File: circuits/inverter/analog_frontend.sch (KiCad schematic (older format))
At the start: 104 parts

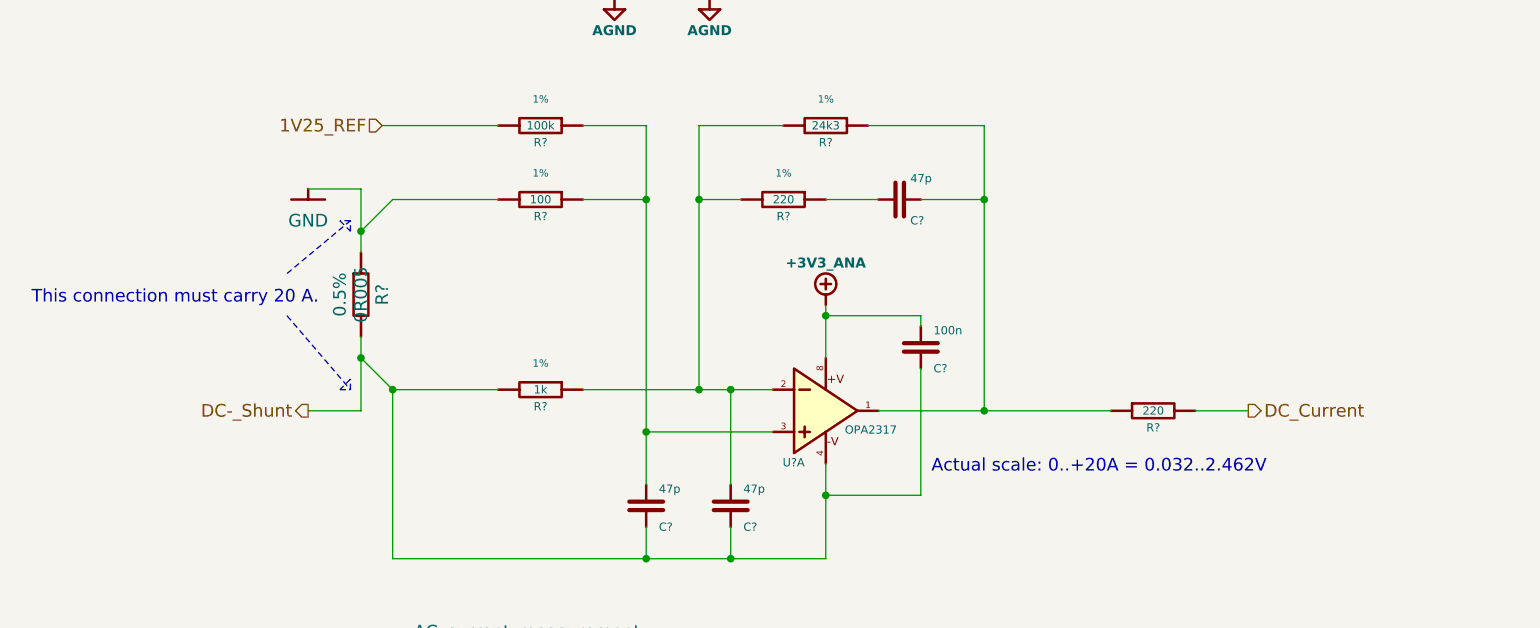
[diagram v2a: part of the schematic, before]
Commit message: fixes power symbols and pin attributes in library,
adds various footprints
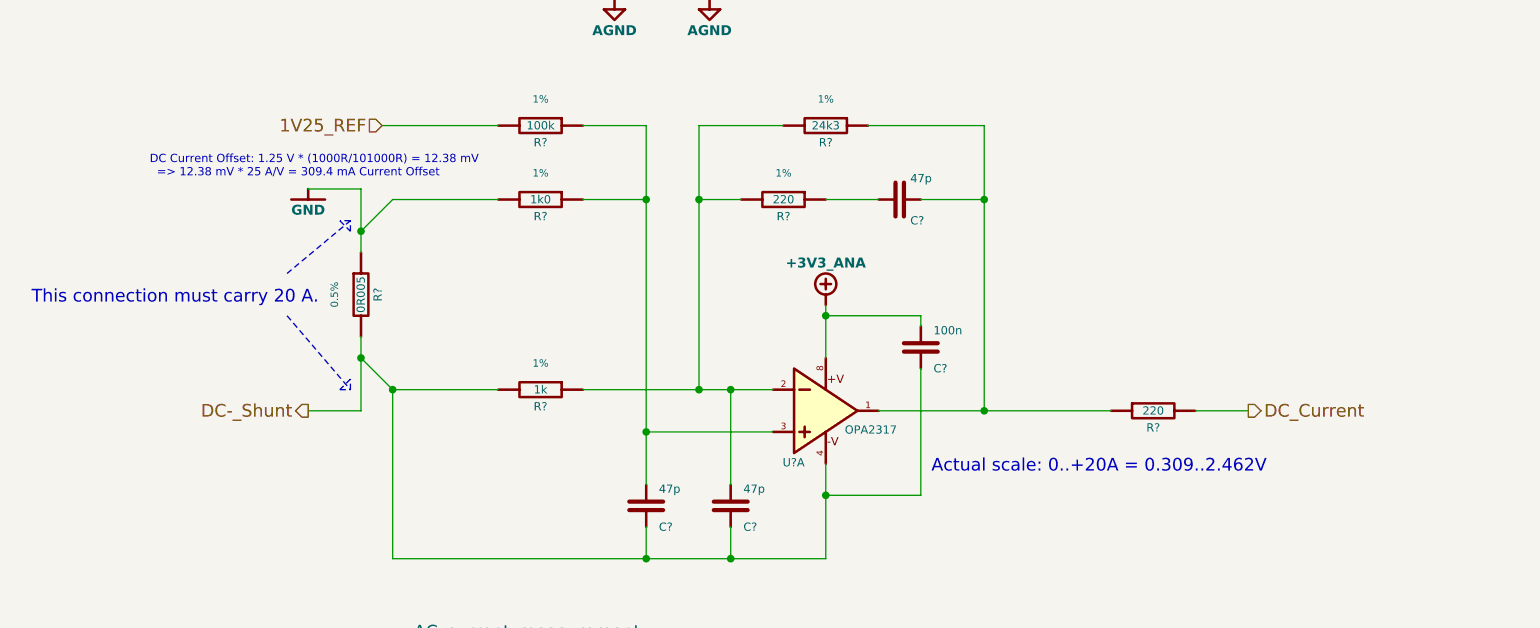
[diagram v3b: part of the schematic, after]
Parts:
- removed R?: 0R005, symbol Resistor
- added R?: 0R005, symbol Resistor
- R?: value 100 -> 1k0
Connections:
- net DC-_Shunt: now also R?.2
- net at R?.2: now also R?.1
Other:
- note added: "Actual scale: 0..+20A = 0.309..2.462V"
- note added: "DC Current Offset: 1.25 V * (1000R/101000R) = 12.38 mV\n => 12.38 mV * 25 A/V = 309.4 mA Current Offset"
- note removed: "Actual scale: 0..+20A = 0.032..2.462V"
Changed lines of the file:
@@
 	14500 7150 14750 7150
 Text Notes 13250 7450 0    60   ~ 0
-Actual scale: 0..+20A = 0.032..2.462V
-$Comp
-L GND #GND044
-U 1 1 56E375C1
-P 10300 6100
-F 0 "#GND044" H 10300 5800 60  0001 C CNN
-F 1 "GND" H 10300 5950 60  0000 C CNN
-F 2 "" H 10300 6100 60  0000 C CNN
-F 3 "" H 10300 6100 60  0000 C CNN
-	1    10300 6100
-	1    0    0    -1
-$EndComp
+Actual scale: 0..+20A = 0.309..2.462V
 Text HLabel 10300 7150 0    60   Output ~ 0
 DC-_Shunt
-$Comp
-L Resistor R?
-U 1 1 56E37B4F
-P 10550 6600
-F 0 "R?" H 10550 6500 60  0000 C CNN
-F 1 "0R005" H 10550 6600 60  0000 C CNN
-F 2 "" H 10550 6690 60  0001 R CNN
-F 3 "" H 10550 6600 60  0000 C CNN
-F 4 "0.5%" H 10550 6700 60  0000 C CNN "Tolerance"
-F 5 "M" H 10725 6800 60  0001 L CNN "Manufacturer"
-F 6 "P" H 10725 6700 60  0001 L CNN "Partnumber"
-	1    10550 6600
-	0    -1   1    0
-$EndComp
 Wire Wire Line
 	10300 6100 10550 6100
@@
 P 11400 6150
 F 0 "R?" H 11400 6070 39  0000 C CNN
-F 1 "100" H 11400 6150 39  0000 C CNN
+F 1 "1k0" H 11400 6150 39  0000 C CNN
 F 2 "" H 11400 6220 35  0000 C CNN
 F 3 "" H 11400 6150 60  0000 C CNN
@@
 	1    0    0    -1
 $EndComp
+Text Notes 9550 6050 0    39   ~ 0
+DC Current Offset: 1.25 V * (1000R/101000R) = 12.38 mV\n  => 12.38 mV * 25 A/V = 309.4 mA Current Offset
+$Comp
+L Resistor R?
+U 1 1 58D98DA2
+P 10550 6600
+F 0 "R?" H 10550 6520 39  0000 C CNN
+F 1 "0R005" H 10550 6600 39  0000 C CNN
+F 2 "" H 10550 6670 35  0000 C CNN
+F 3 "" H 10550 6600 60  0000 C CNN
+F 4 "0.5%" H 10550 6725 35  0000 C CNN "Tolerance"
+F 5 "M" H 10675 6725 35  0001 L CNN "Manufacturer"
+F 6 "P" H 10675 6675 35  0001 L CNN "Partnumber"
+F 7 "S" H 10675 6775 35  0001 L CNN "Supplier"
+F 8 "O.No." H 10675 6825 35  0001 L CNN "Order No."
+	1    10550 6600
+	0    -1   1    0
+$EndComp
+$Comp
+L GND #GND?
+U 1 1 58D9B0A6
+P 10300 6100
+F 0 "#GND?" H 10300 5910 60  0001 C CNN
+F 1 "GND" H 10300 6000 47  0000 C CNB
+F 2 "" H 10300 6100 60  0000 C CNN
+F 3 "" H 10300 6100 60  0000 C CNN
+	1    10300 6100
+	1    0    0    -1
+$EndComp

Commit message: bulk-updates libraries and schematics
schematic is updated to Kicad 5.1.14
updates various sheets with new circuits
adds various component libraries
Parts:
- C? (x25): symbol Capacitor -> OSSI_standard_components:Capacitor
- R? (x71): symbol Resistor -> OSSI_standard_components:Resistor
- U? (x8): symbol DUAL_OPAMP -> OSSI_standard_components:DUAL_OPAMP
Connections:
- net AGND: now reaches R?.2
- net AGND: now also C?.1, C?.1, C?.1, C?.1, C?.1, C?.1, C?.1, C?.1, C?.1, R?.2, R?.2, U?.4, U?.4, U?.4
- net +3V3: now reaches C?.2, U?.8
- net +3V3: now also C?.2, C?.2, C?.2, U?.8, U?.8, U?.8
- net GND: now reaches R?.1, R?.2

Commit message: minor updates and cleaup
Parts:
- C?, R? (x4): footprint (none) -> OSSI_standard_footprints:0603_W
- R? (x32): footprint (none) -> OSSI_standard_footprints:MELF_0204_W
- R?: value 0R005 -> 5mΩ; footprint (none) -> OSSI_standard_footprints:2512_W; Manufacturer M -> Riedon; Order No. O.No. -> 696-1837-1-ND; Partnumber P -> CSRL3-0R005F8; Supplier S -> Digikey; Tolerance 0.5% -> 1%
- U? (x8): footprint (none) -> OSSI_standard_footprints:SOIC8
